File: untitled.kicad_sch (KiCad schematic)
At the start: 15 parts, among them IC5 HX711, J15 Conn_01x05, Q2 MMBT4403

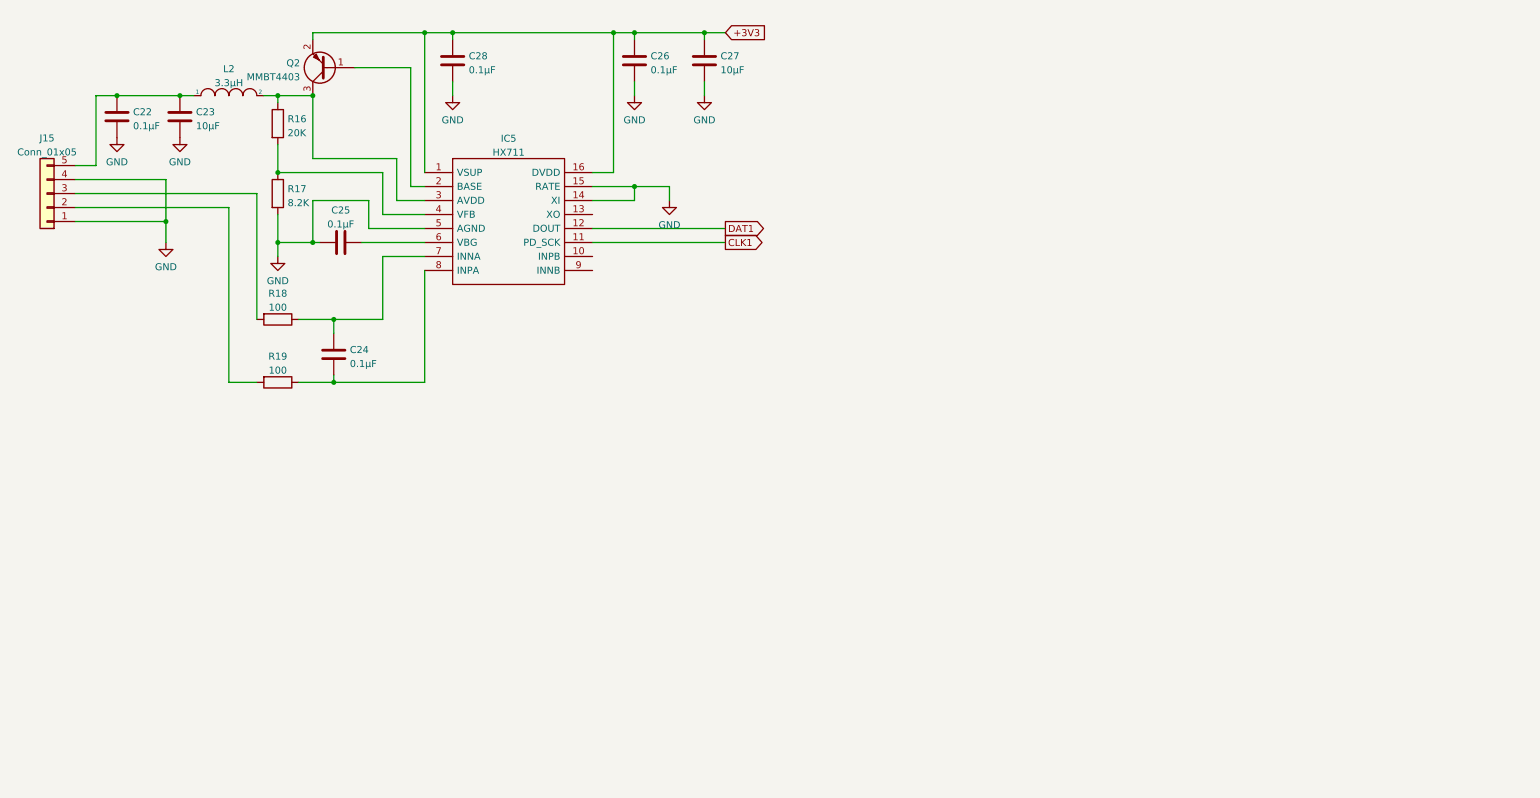
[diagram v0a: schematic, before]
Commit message: Added HX711
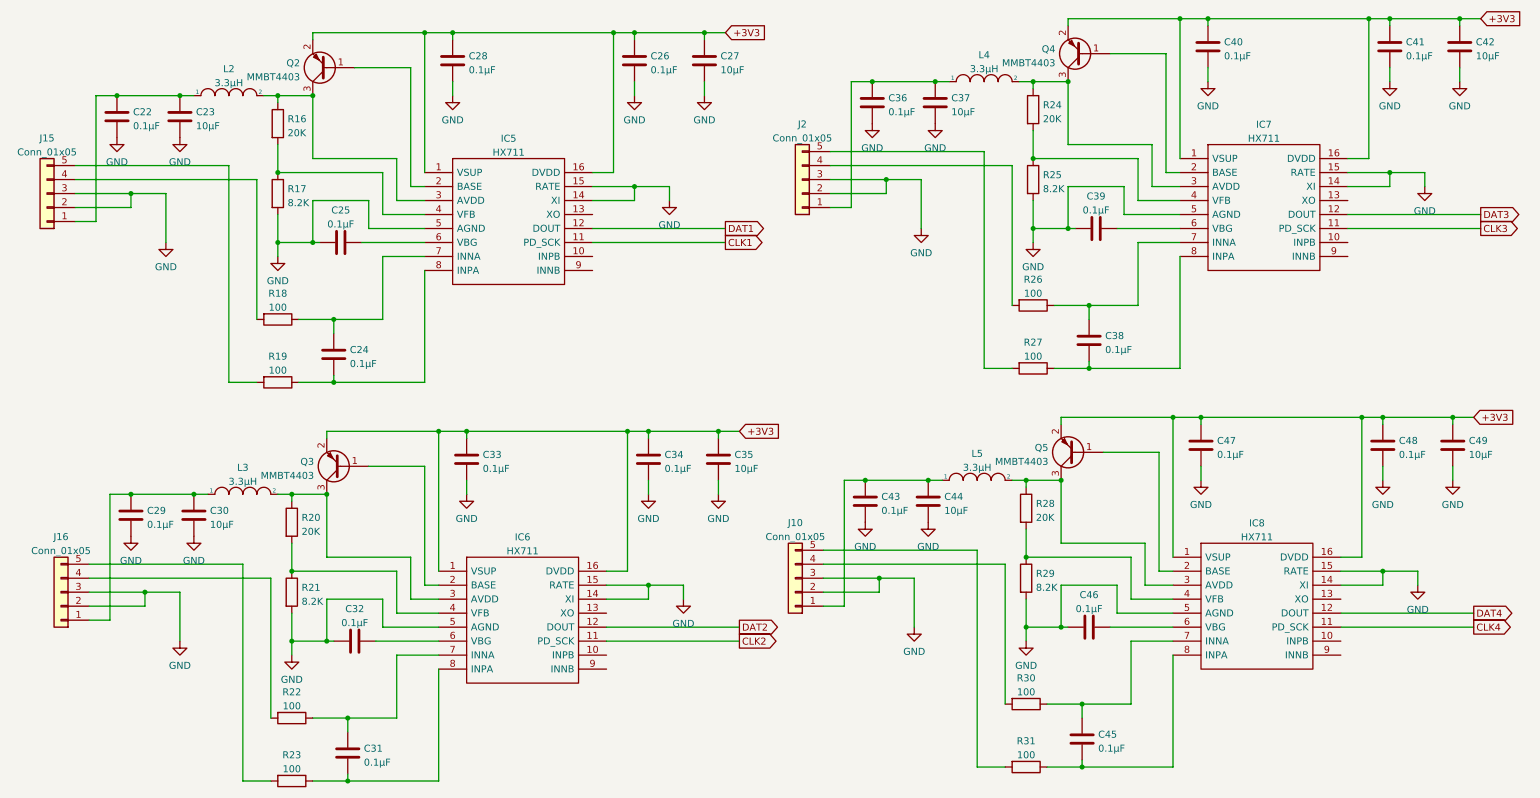
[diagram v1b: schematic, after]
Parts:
- added C29, C31, C32, C33, C34, C36, C38, C39, C40, C41, C43, C45, C46, C47, C48: 0.1µF, Capacitor_SMD:C_0603_1608Metric, symbol Device:C
- added C30, C35, C37, C42, C44, C49: 10µF, Capacitor_SMD:C_0805_2012Metric, symbol Device:C
- added IC6, IC7, IC8: HX711, Empreintes:SOIC127P600X160-16N, symbol HX711:HX711
- added J10, J16, J2: Conn_01x05, Empreintes:connecteurs5, symbol Connector_Generic:Conn_01x05
- added L3, L4, L5: 3.3µH, Inductor_SMD:L_0603_1608Metric, symbol pspice:INDUCTOR
- added Q3, Q4, Q5: MMBT4403, Package_TO_SOT_SMD:SOT-23, symbol Transistor_BJT:MMBTA92
- added R20, R24, R28: 20K, Resistor_SMD:R_0603_1608Metric, symbol Device:R
- added R21, R25, R29: 8.2K, Resistor_SMD:R_0603_1608Metric, symbol Device:R
- added R22, R23, R26, R27, R30, R31: 100, Resistor_SMD:R_0603_1608Metric, symbol Device:R
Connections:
- net +3V3: now also C33.1, C34.1, C35.1, C40.1, C41.1, C42.1, C47.1, C48.1, C49.1, IC6.1 (VSUP), IC6.16 (DVDD), IC7.1 (VSUP), IC7.16 (DVDD), IC8.1 (VSUP), IC8.16 (DVDD), Q3.2 (E), Q4.2 (E), Q5.2 (E)
- net GND: now also J15.2 (Pin_2), J15.3 (Pin_3), C29.2, C30.2, C32.1, C33.2, C34.2, C35.2, C36.2, C37.2, C39.1, C40.2, C41.2, C42.2, C43.2, C44.2, C46.1, C47.2, C48.2, C49.2, IC6.14 (XI), IC6.15 (RATE), IC6.5 (AGND), IC7.14 (XI), IC7.15 (RATE), IC7.5 (AGND), IC8.14 (XI), IC8.15 (RATE), IC8.5 (AGND), J10.2 (Pin_2), J10.3 (Pin_3), J16.2 (Pin_2), J16.3 (Pin_3), J2.2 (Pin_2), J2.3 (Pin_3), R21.2, R25.2, R29.2; no longer J15.1 (Pin_1), J15.4 (Pin_4)
- net at C22.1, C23.1, L2.1: now also J15.1 (Pin_1); no longer J15.5 (Pin_5)
- net at R18.2: now also J15.4 (Pin_4); no longer J15.3 (Pin_3)
- net at R19.2: now also J15.5 (Pin_5); no longer J15.2 (Pin_2)
- new net: C43.1, C44.1, J10.1 (Pin_1), L5.1
- new net: IC8.3 (AVDD), L5.2, Q5.3 (C), R28.1
- new net: IC8.4 (VFB), R28.2, R29.1
- new net: IC7.2 (BASE), Q4.1 (B)
- new net: IC7.3 (AVDD), L4.2, Q4.3 (C), R24.1
- new net: IC7.4 (VFB), R24.2, R25.1
- new net: IC8.2 (BASE), Q5.1 (B)
- new net: C39.2, IC7.6 (VBG)
- new net: C31.1, IC6.7 (INNA), R22.1
- new net: C31.2, IC6.8 (INPA), R23.1
- new net: C29.1, C30.1, J16.1 (Pin_1), L3.1
- new net: IC6.3 (AVDD), L3.2, Q3.3 (C), R20.1
- new net: J16.5 (Pin_5), R23.2
- new net: C36.1, C37.1, J2.1 (Pin_1), L4.1
- new net: J2.4 (Pin_4), R26.2
- new net: J2.5 (Pin_5), R27.2
- new net: C45.1, IC8.7 (INNA), R30.1
- new net: J10.4 (Pin_4), R30.2
- new net: IC6.4 (VFB), R20.2, R21.1
- new net: IC6.2 (BASE), Q3.1 (B)
- new net: C32.2, IC6.6 (VBG)
- new net: C38.1, IC7.7 (INNA), R26.1
- new net: C38.2, IC7.8 (INPA), R27.1
- new net: J10.5 (Pin_5), R31.2
- new net: C46.2, IC8.6 (VBG)
- new net: C45.2, IC8.8 (INPA), R31.1
- new net: J16.4 (Pin_4), R22.2
- new net CLK2: IC6.11 (PD_SCK)
- new net CLK3: IC7.11 (PD_SCK)
- new net CLK4: IC8.11 (PD_SCK)
- new net DAT2: IC6.12 (DOUT)
- new net DAT3: IC7.12 (DOUT)
- new net DAT4: IC8.12 (DOUT)

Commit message: Update
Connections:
- net +3V3 renamed VCC
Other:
- moved on the sheet: J15
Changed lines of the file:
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@@
     (stroke (width 0) (type default) (color 0 0 0 0))
   )
-  (wire (pts (xy 54.61 43.18) (xy 21.59 43.18))
+  (wire (pts (xy 54.61 43.18) (xy 22.86 43.18))
     (stroke (width 0) (type default) (color 0 0 0 0))
   )
@@
     (stroke (width 0) (type default) (color 0 0 0 0))
   )
-  (wire (pts (xy 31.75 45.72) (xy 21.59 45.72))
+  (wire (pts (xy 31.75 45.72) (xy 22.86 45.72))
     (stroke (width 0) (type default) (color 0 0 0 0))
   )
@@
     (stroke (width 0) (type default) (color 0 0 0 0))
   )
-  (wire (pts (xy 21.59 48.26) (xy 31.75 48.26))
+  (wire (pts (xy 22.86 48.26) (xy 31.75 48.26))
     (stroke (width 0) (type default) (color 0 0 0 0))
   )
@@
     (stroke (width 0) (type default) (color 0 0 0 0))
   )
-  (wire (pts (xy 21.59 40.64) (xy 49.53 40.64))
+  (wire (pts (xy 22.86 40.64) (xy 49.53 40.64))
     (stroke (width 0) (type default) (color 0 0 0 0))
   )
@@
     (stroke (width 0) (type default) (color 0 0 0 0))
   )
-  (wire (pts (xy 25.4 50.8) (xy 21.59 50.8))
+  (wire (pts (xy 25.4 50.8) (xy 22.86 50.8))
     (stroke (width 0) (type default) (color 0 0 0 0))
   )
@@
     )
   )
-  (global_label "+3V3" (shape input) (at 276.86 13.97 0) (fields_autoplaced)
+  (global_label "VCC" (shape input) (at 276.86 13.97 0) (fields_autoplaced)
     (effects (font (size 1.27 1.27)) (justify left))
-    (property "Intersheet References" "${INTERSHEET_REFS}" (id 0) (at 284.2642 13.8906 0)
-      (effects (font (size 1.27 1.27)) (justify left) hide)
-    )
-  )
-  (global_label "+3V3" (shape input) (at 275.59 86.36 0) (fields_autoplaced)
+    (property "Intersheet References" "${INTERSHEET_REFS}" (id 0) (at 282.8128 13.8906 0)
+      (effects (font (size 1.27 1.27)) (justify left) hide)
+    )
+  )
+  (global_label "VCC" (shape input) (at 275.59 86.36 0) (fields_autoplaced)
     (effects (font (size 1.27 1.27)) (justify left))
-    (property "Intersheet References" "${INTERSHEET_REFS}" (id 0) (at 282.9942 86.2806 0)
-      (effects (font (size 1.27 1.27)) (justify left) hide)
-    )
-  )
-  (global_label "+3V3" (shape input) (at 139.7 16.51 0) (fields_autoplaced)
+    (property "Intersheet References" "${INTERSHEET_REFS}" (id 0) (at 281.5428 86.2806 0)
+      (effects (font (size 1.27 1.27)) (justify left) hide)
+    )
+  )
+  (global_label "VCC" (shape input) (at 139.7 16.51 0) (fields_autoplaced)
     (effects (font (size 1.27 1.27)) (justify left))
-    (property "Intersheet References" "${INTERSHEET_REFS}" (id 0) (at 147.1042 16.4306 0)
+    (property "Intersheet References" "${INTERSHEET_REFS}" (id 0) (at 145.6528 16.4306 0)
       (effects (font (size 1.27 1.27)) (justify left) hide)
     )
@@
     )
   )
-  (global_label "+3V3" (shape input) (at 142.24 88.9 0) (fields_autoplaced)
+  (global_label "VCC" (shape input) (at 142.24 88.9 0) (fields_autoplaced)
     (effects (font (size 1.27 1.27)) (justify left))
-    (property "Intersheet References" "${INTERSHEET_REFS}" (id 0) (at 149.6442 88.8206 0)
+    (property "Intersheet References" "${INTERSHEET_REFS}" (id 0) (at 148.1928 88.8206 0)
       (effects (font (size 1.27 1.27)) (justify left) hide)
     )
@@
     (pin "2")
   )
-  (symbol (lib_id "Connector_Generic:Conn_01x05") (at 16.51 45.72 180) (unit 1)
-    (in_bom yes) (on_board yes) (fields_autoplaced)
-    (property "Reference" "J15" (id 0) (at 16.51 35.6702 0))
-    (property "Value" "Conn_01x05" (id 1) (at 16.51 38.2071 0))
-    (property "Footprint" "Empreintes:connecteurs5" (id 2) (at 16.51 45.72 0)
-      (effects (font (size 1.27 1.27)) hide)
-    )
-    (property "Datasheet" "~" (id 3) (at 16.51 45.72 0)
-      (effects (font (size 1.27 1.27)) hide)
-    )
+  (symbol (lib_id "Connector_Generic:Conn_01x05") (at 17.78 45.72 180) (unit 1)
+    (in_bom yes) (on_board yes) (fields_autoplaced)
+    (property "Reference" "J15" (id 0) (at 17.78 35.6702 0))
+    (property "Value" "Conn_01x05" (id 1) (at 17.78 38.2071 0))
+    (property "Footprint" "Empreintes:connecteurs5" (id 2) (at 17.78 45.72 0)
+      (effects (font (size 1.27 1.27)) hide)
+    )
+    (property "Datasheet" "~" (id 3) (at 17.78 45.72 0)
+      (effects (font (size 1.27 1.27)) hide)
+    )
